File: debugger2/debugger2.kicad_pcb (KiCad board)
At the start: 2 copper layers, 65 x 30 mm, 63 parts, among them IC1 AT24CS32-SSHM, P1 CONN_01X01, P2 CONN_01X01, P3 USB_OTG, P4 CONN_02X20, P5 CONN_01X02, Q1 Q_PMOS_GSD, Q2 DMMT3906_Dual_PNP, U1 93LC56B, U2 MIC9409x_SC-70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

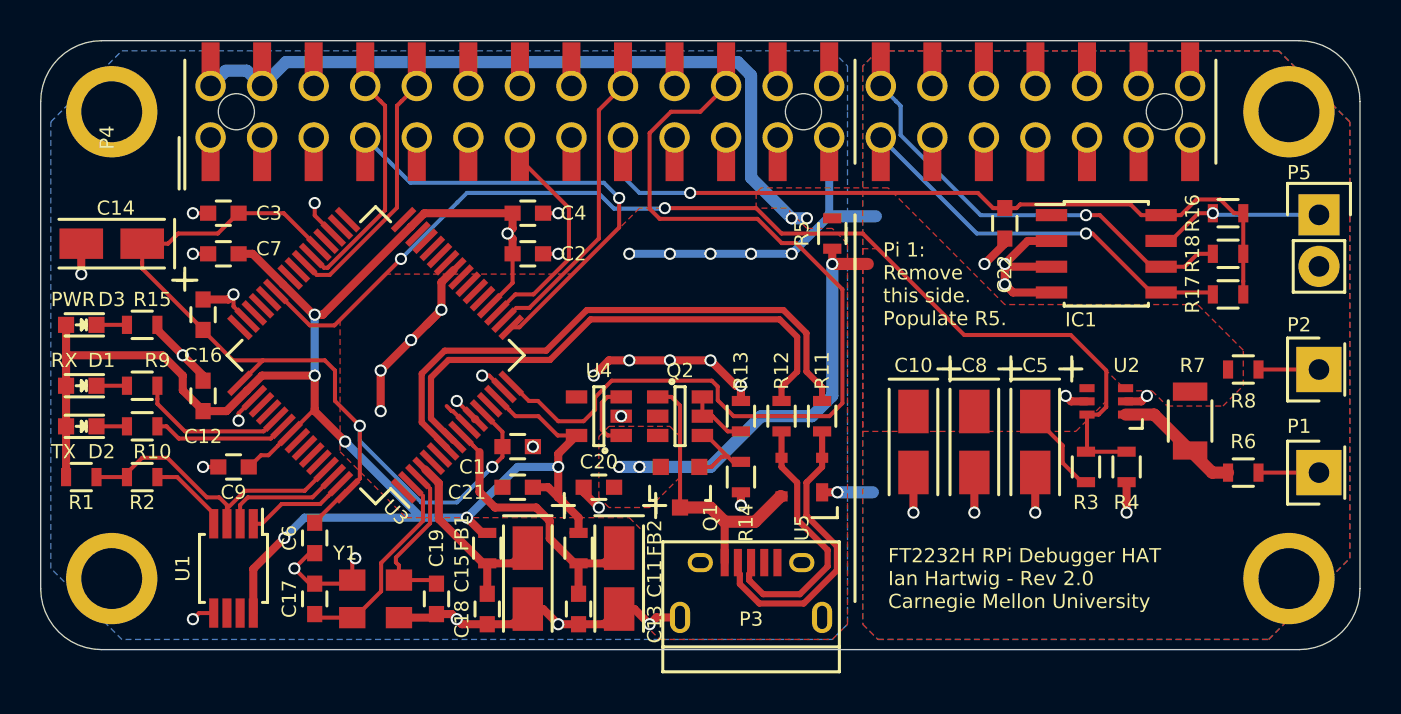
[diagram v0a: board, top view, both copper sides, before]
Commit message: update board layout for 6/6mil (was 5/5mil)
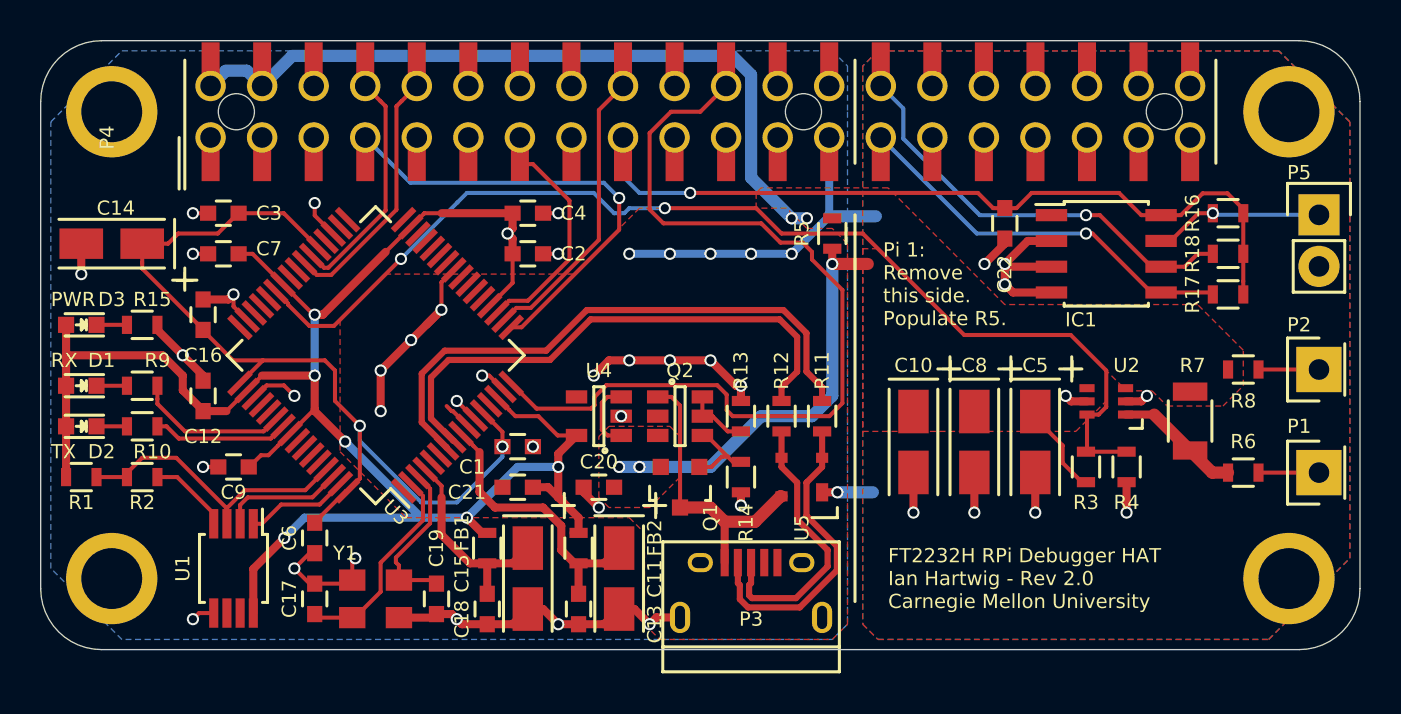
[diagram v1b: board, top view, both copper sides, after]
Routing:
- net GND: track 112.0 -> 113.0 mm
- net /RPI_3V3_2: track 39.3 -> 40.2 mm
- net /FT_EEDATA: track 15.3 -> 14.4 mm
- net /USB_D-: track 14.7 -> 15.3 mm
- net /USB_D+: track 13.2 -> 13.8 mm
- net Net-(C15-Pad1): track 9.82 -> 10.4 mm
- net /GPIO25_TCK: track 46.2 -> 45.6 mm
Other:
- net class Default: clearance 0.127 -> 0.1524
- net class PiPower: clearance 0.127 -> 0.1524
- net class Power: clearance 0.127 -> 0.1524
- net class USB: clearance 0.127 -> 0.1524
- rule trace_clearance: 0.127 -> 0.1524
- rule trace_min: 0.127 -> 0.1522
- rule via_min_drill: 0.3 -> 0.3048
